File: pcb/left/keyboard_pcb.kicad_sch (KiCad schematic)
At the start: 101 parts, among them J3 Alt. Battery, J4 Conn_01x01_Socket, K00 KEYSW, K01 KEYSW, K02 KEYSW, K03 KEYSW, K04 KEYSW, K05 KEYSW, K10 KEYSW, K11 KEYSW, K12 KEYSW, K13 KEYSW, K14 KEYSW, K15 KEYSW, K20 KEYSW, K21 KEYSW, K22 KEYSW, K23 KEYSW, K24 KEYSW, K25 KEYSW, K33 KEYSW, K34 KEYSW, K35 KEYSW, U1 Flippable RP2040 ProMicro/nic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

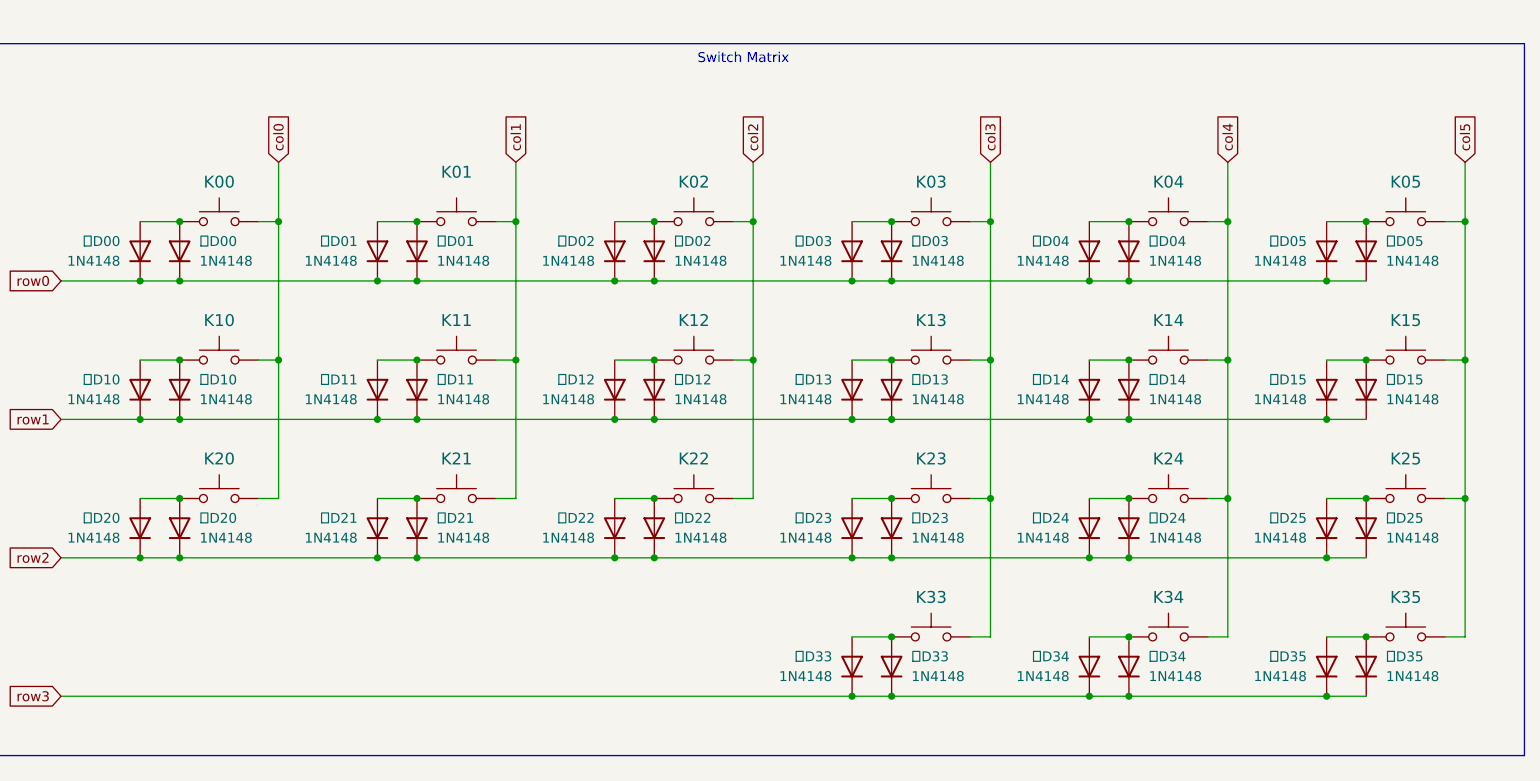
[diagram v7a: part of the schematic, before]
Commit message: Update matrix to remove missing connections
The switch side of lefthand diodes no longer need to connect righthand diodes. Diodes join to the same row trace, but the switch-to-diode connections are separate (except for the switches that overlap with nav. switches — these are joined to reduct routes). The switches in the schematic are now represented as SPDT switches, which have two outputs instead of one. The footprints have been updated to number the righthand side leg to pin 3 (instead of being another pin 1).
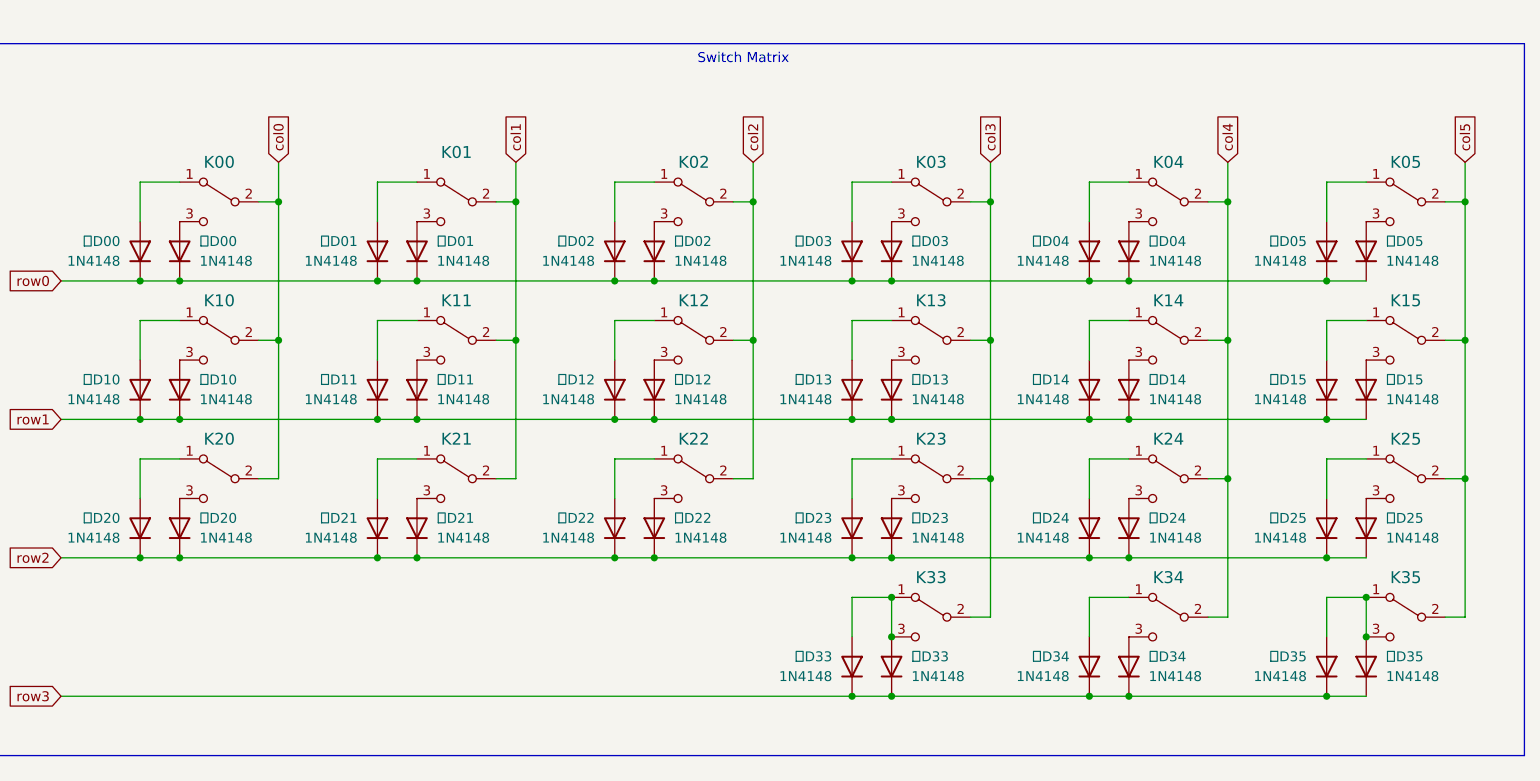
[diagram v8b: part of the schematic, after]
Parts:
- K00, K01, K02, K03, K04, K05, K10, K11, K12, K13, K14, K15, K20, K21, K22, K23, K24, K25, K33, K34, K35: symbol Switch:SW_Push -> Switch:SW_SPDT
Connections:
- net at K35.1 (A), 右D35.2 (A), 左D35.2 (A): now also K35.3 (C)
- net at K13.1 (A), 左D13.2 (A): no longer 右D13.2 (A)
- net at K01.1 (A), 左D01.2 (A): no longer 右D01.2 (A)
- net at K24.1 (A), 左D24.2 (A): no longer 右D24.2 (A)
- net at K05.1 (A), 左D05.2 (A): no longer 右D05.2 (A)
- net at K04.1 (A), 左D04.2 (A): no longer 右D04.2 (A)
- net at K20.1 (A), 左D20.2 (A): no longer 右D20.2 (A)
- net at K11.1 (A), 左D11.2 (A): no longer 右D11.2 (A)
- net at K25.1 (A), 左D25.2 (A): no longer 右D25.2 (A)
- net at K00.1 (A), 左D00.2 (A): no longer 右D00.2 (A)
- net at K14.1 (A), 左D14.2 (A): no longer 右D14.2 (A)
- net at K15.1 (A), 左D15.2 (A): no longer 右D15.2 (A)
- net at K23.1 (A), 左D23.2 (A): no longer 右D23.2 (A)
- net at K12.1 (A), 左D12.2 (A): no longer 右D12.2 (A)
- net at K03.1 (A), 左D03.2 (A): no longer 右D03.2 (A)
- net at K22.1 (A), 左D22.2 (A): no longer 右D22.2 (A)
- net at K02.1 (A), 左D02.2 (A): no longer 右D02.2 (A)
- net at K33.1 (A), 右D33.2 (A), 左D33.2 (A): now also K33.3 (C)
- net at K10.1 (A), 左D10.2 (A): no longer 右D10.2 (A)
- net at K34.1 (A), 左D34.2 (A): no longer 右D34.2 (A)
- net at K21.1 (A), 左D21.2 (A): no longer 右D21.2 (A)
- new net: K01.3 (C), 右D01.2 (A)
- new net: K04.3 (C), 右D04.2 (A)
- new net: K25.3 (C), 右D25.2 (A)
- new net: K24.3 (C), 右D24.2 (A)
- new net: K00.3 (C), 右D00.2 (A)
- new net: K15.3 (C), 右D15.2 (A)
- new net: K23.3 (C), 右D23.2 (A)
- new net: K12.3 (C), 右D12.2 (A)
- new net: K03.3 (C), 右D03.2 (A)
- new net: K02.3 (C), 右D02.2 (A)
- new net: K11.3 (C), 右D11.2 (A)
- new net: K22.3 (C), 右D22.2 (A)
- new net: K20.3 (C), 右D20.2 (A)
- new net: K10.3 (C), 右D10.2 (A)
- new net: K34.3 (C), 右D34.2 (A)
- new net: K13.3 (C), 右D13.2 (A)
- new net: K14.3 (C), 右D14.2 (A)
- new net: K05.3 (C), 右D05.2 (A)
- new net: K21.3 (C), 右D21.2 (A)
